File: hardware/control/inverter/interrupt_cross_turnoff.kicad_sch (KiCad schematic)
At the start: 17 parts, among them J1 RJ45, J2 RJ45, J3 RJ45, U1 L7812, U2 L7805, U3 74HC14, U4 74HC08, U5 74HC74

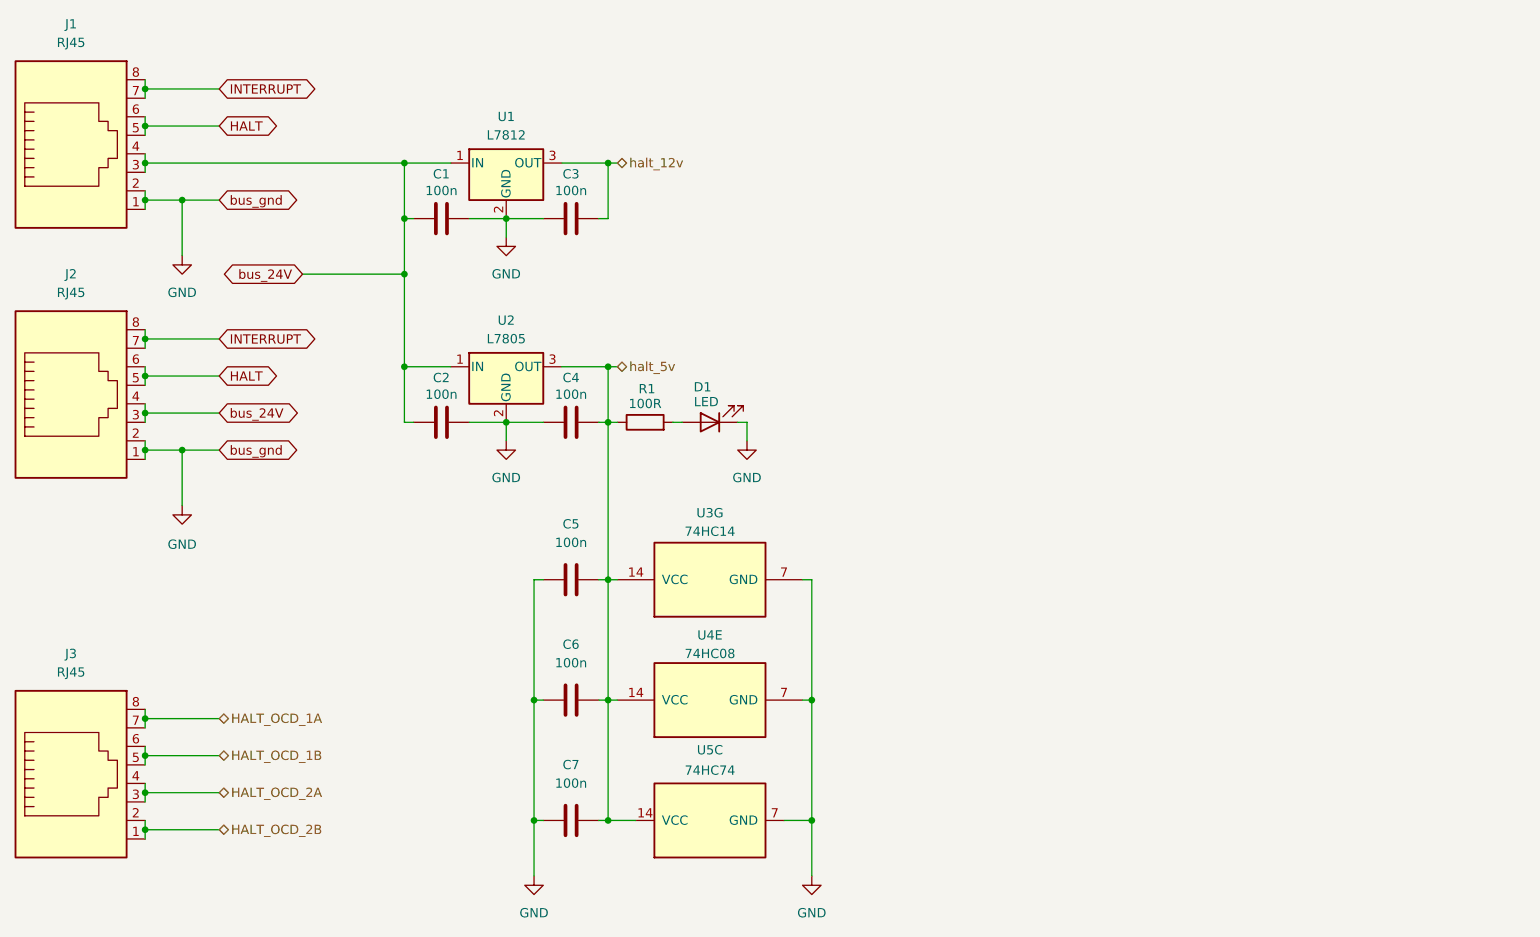
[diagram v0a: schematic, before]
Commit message: add progress on main drive controller and switch to hiearchical labels
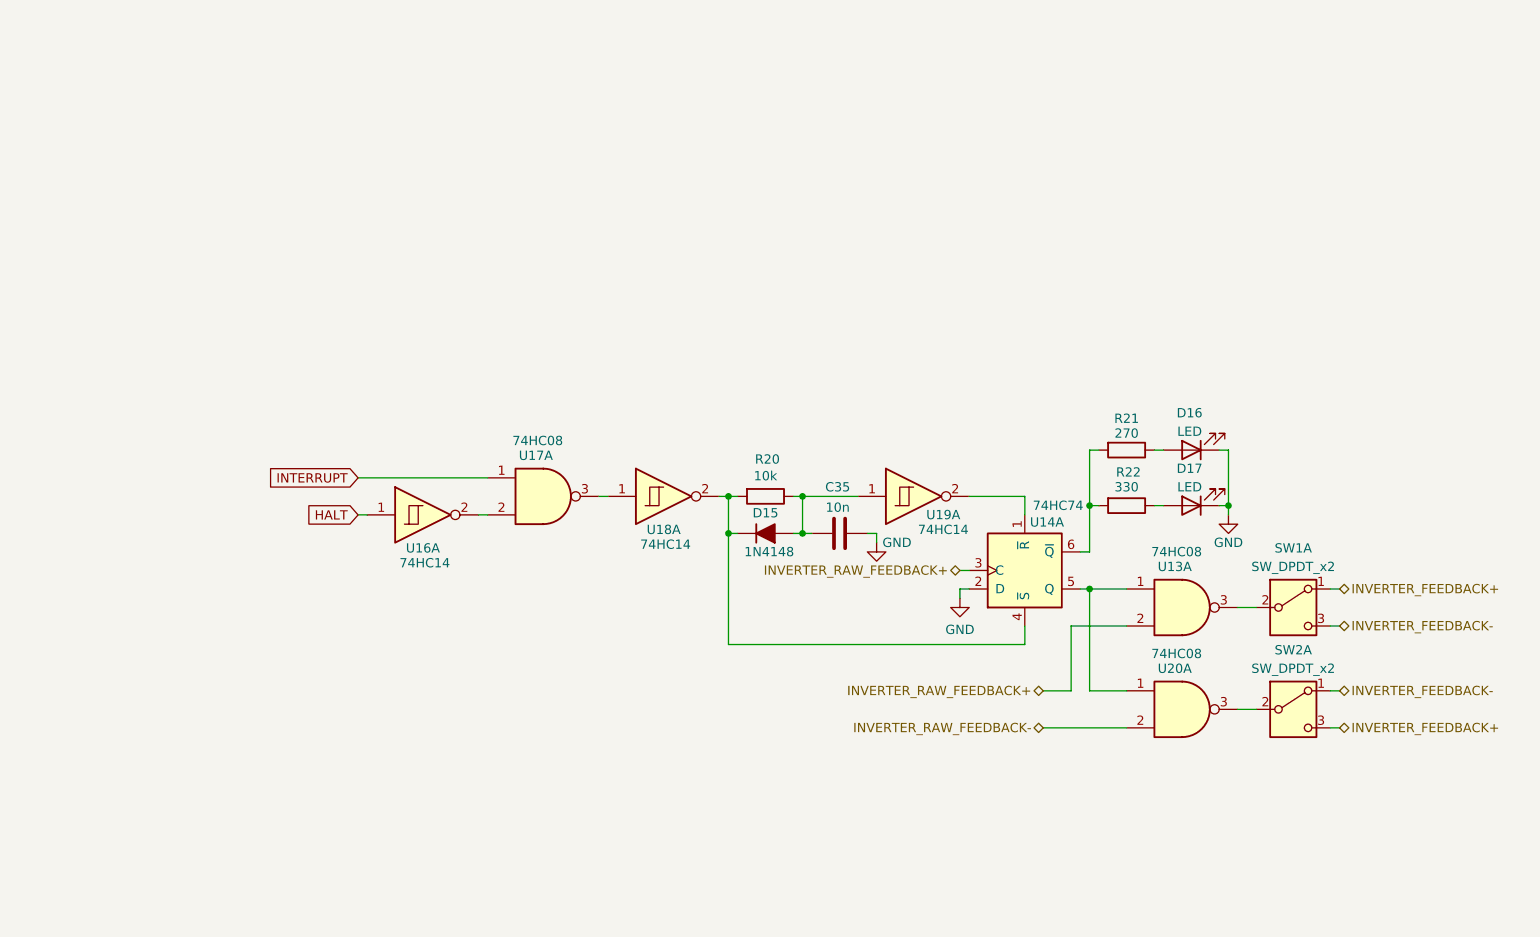
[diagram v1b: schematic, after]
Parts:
- removed C1, C2, C3, C4, C5, C6, C7: 100n, symbol Device:C
- removed D1: LED, symbol Device:LED
- removed J1, J2, J3: RJ45, symbol Connector:RJ45
- removed R1: 100R, symbol Device:R
- removed U1: L7812, symbol Regulator_Linear:L7812
- removed U2: L7805, symbol Regulator_Linear:L7805
- removed U3: 74HC14, symbol 74xx:74HC14
- removed U4: 74HC08, symbol 74xx:74HC00
- removed U5: 74HC74, symbol 74xx:74HC74
- added C35: 10n, symbol Device:C
- added D15: 1N4148, PCM_Diode_THT_AKL:D_DO-35_SOD27_P7.62mm_Horizontal, symbol PCM_Diode_AKL:1N4148
- added D16, D17: LED, symbol Device:LED
- added R20: 10k, symbol Device:R
- added R21: 270, symbol Device:R
- added R22: 330, symbol Device:R
- added SW1, SW2: SW_DPDT_x2, symbol Switch:SW_DPDT_x2
- added U13, U17, U20: 74HC08, symbol 74xx:74HC00
- added U14: 74HC74, symbol 74xx:74HC74
- added U16, U18, U19: 74HC14, symbol 74xx:74HC14
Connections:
- net GND: now also C35.2, D16.1 (K), D17.1 (K), U14.2 (D)
- net HALT: now also U16.1
- net INTERRUPT: now also U17.1
- new net: C35.1, D15.2 (A), R20.1, U19.1
- new net: D15.1 (K), R20.2, U14.4 (~{S}), U18.2
- new net: U13.1, U14.5 (Q), U20.1
- new net: SW2.2 (B), U20.3
- new net: D17.2 (A), R22.1
- new net: R21.2, R22.2, U14.6 (~{Q})
- new net: D16.2 (A), R21.1
- new net: U14.1 (~{R}), U19.2
- new net: SW1.2 (B), U13.3
- new net: U16.2, U17.2
- new net: U17.3, U18.1
- new net INVERTER_FEEDBACK+: SW1.1 (A), SW2.3 (C)
- new net INVERTER_FEEDBACK-: SW1.3 (C), SW2.1 (A)
- new net INVERTER_RAW_FEEDBACK+: U13.2, U14.3 (C)
- new net INVERTER_RAW_FEEDBACK-: U20.2
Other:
- company: Author: 9551 (devvie.cc) -> (none)
- title: QCW DRSSTC halt board input stage -> (none)

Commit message: update
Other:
- moved on the sheet: SW1A, SW2A, U13A, U20A
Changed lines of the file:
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@@
 	)
 	(junction
-		(at 167.64 102.87)
+		(at 167.64 111.76)
 		(diameter 0)
 		(color 0 0 0 0)
@@
 	(wire
 		(pts
-			(xy 167.64 102.87) (xy 167.64 116.84)
+			(xy 167.64 111.76) (xy 167.64 125.73)
 		)
 		(stroke
@@
 	(wire
 		(pts
+			(xy 167.64 102.87) (xy 166.37 102.87)
+		)
+		(stroke
+			(width 0)
+			(type default)
+		)
+	)
+	(wire
+		(pts
 			(xy 100.33 90.17) (xy 101.6 90.17)
 		)
@@
 	(wire
 		(pts
-			(xy 165.1 107.95) (xy 172.72 107.95)
-		)
-		(stroke
-			(width 0)
-			(type default)
-		)
-	)
-	(wire
-		(pts
 			(xy 118.11 90.17) (xy 119.38 90.17)
 		)
@@
 	(wire
 		(pts
-			(xy 166.37 102.87) (xy 167.64 102.87)
-		)
-		(stroke
-			(width 0)
-			(type default)
-		)
-	)
-	(wire
-		(pts
 			(xy 185.42 91.44) (xy 186.69 91.44)
 		)
@@
 	(wire
 		(pts
-			(xy 187.96 119.38) (xy 190.5 119.38)
+			(xy 184.15 128.27) (xy 186.69 128.27)
 		)
 		(stroke
@@
 	(wire
 		(pts
-			(xy 161.29 116.84) (xy 165.1 116.84)
+			(xy 161.29 116.84) (xy 168.91 116.84)
 		)
 		(stroke
@@
 	(wire
 		(pts
-			(xy 167.64 102.87) (xy 172.72 102.87)
+			(xy 167.64 111.76) (xy 168.91 111.76)
 		)
 		(stroke
@@
 	(wire
 		(pts
-			(xy 165.1 116.84) (xy 165.1 107.95)
-		)
-		(stroke
-			(width 0)
-			(type default)
-		)
-	)
-	(wire
-		(pts
 			(xy 138.43 95.25) (xy 138.43 96.52)
 		)
@@
 	(wire
 		(pts
-			(xy 167.64 116.84) (xy 172.72 116.84)
-		)
-		(stroke
-			(width 0)
-			(type default)
-		)
-	)
-	(wire
-		(pts
-			(xy 200.66 107.95) (xy 201.93 107.95)
-		)
-		(stroke
-			(width 0)
-			(type default)
-		)
-	)
-	(wire
-		(pts
-			(xy 200.66 121.92) (xy 201.93 121.92)
+			(xy 167.64 125.73) (xy 168.91 125.73)
+		)
+		(stroke
+			(width 0)
+			(type default)
+		)
+	)
+	(wire
+		(pts
+			(xy 196.85 116.84) (xy 198.12 116.84)
+		)
+		(stroke
+			(width 0)
+			(type default)
+		)
+	)
+	(wire
+		(pts
+			(xy 196.85 130.81) (xy 198.12 130.81)
 		)
 		(stroke
@@
 	(wire
 		(pts
-			(xy 200.66 102.87) (xy 201.93 102.87)
-		)
-		(stroke
-			(width 0)
-			(type default)
-		)
-	)
-	(wire
-		(pts
-			(xy 161.29 121.92) (xy 172.72 121.92)
+			(xy 167.64 111.76) (xy 167.64 102.87)
+		)
+		(stroke
+			(width 0)
+			(type default)
+		)
+	)
+	(wire
+		(pts
+			(xy 196.85 111.76) (xy 198.12 111.76)
+		)
+		(stroke
+			(width 0)
+			(type default)
+		)
+	)
+	(wire
+		(pts
+			(xy 161.29 130.81) (xy 168.91 130.81)
 		)
 		(stroke
@@
 	(wire
 		(pts
-			(xy 200.66 116.84) (xy 201.93 116.84)
-		)
-		(stroke
-			(width 0)
-			(type default)
-		)
-	)
-	(wire
-		(pts
-			(xy 187.96 105.41) (xy 190.5 105.41)
+			(xy 196.85 125.73) (xy 198.12 125.73)
+		)
+		(stroke
+			(width 0)
+			(type default)
+		)
+	)
+	(wire
+		(pts
+			(xy 184.15 114.3) (xy 186.69 114.3)
 		)
 		(stroke
@@
 	(hierarchical_label "INVERTER_RAW_FEEDBACK-"
 		(shape bidirectional)
-		(at 161.29 121.92 180)
+		(at 161.29 130.81 180)
 		(effects
 			(font
@@
 	(hierarchical_label "INVERTER_FEEDBACK+"
 		(shape bidirectional)
-		(at 201.93 102.87 0)
+		(at 198.12 111.76 0)
 		(effects
 			(font
@@
 	(hierarchical_label "INVERTER_FEEDBACK-"
 		(shape bidirectional)
-		(at 201.93 107.95 0)
+		(at 198.12 116.84 0)
 		(effects
 			(font
@@
 	(hierarchical_label "INVERTER_FEEDBACK+"
 		(shape bidirectional)
-		(at 201.93 121.92 0)
+		(at 198.12 130.81 0)
 		(effects
 			(font
@@
 	(hierarchical_label "INVERTER_FEEDBACK-"
 		(shape bidirectional)
-		(at 201.93 116.84 0)
+		(at 198.12 125.73 0)
 		(effects
 			(font
@@
 	(symbol
 		(lib_id "74xx:74HC00")
-		(at 180.34 119.38 0)
+		(at 176.53 128.27 0)
 		(unit 1)
 		(exclude_from_sim no)
@@
 		(dnp no)
 		(property "Reference" "U20"
-			(at 179.324 113.792 0)
+			(at 175.514 122.682 0)
 			(effects
 				(font
@@
 		)
 		(property "Value" "74HC08"
-			(at 179.578 111.76 0)
+			(at 175.768 120.65 0)
 			(effects
 				(font
@@
 		)
 		(property "Footprint" ""
-			(at 180.34 119.38 0)
+			(at 176.53 128.27 0)
 			(effects
 				(font
@@
 		)
 		(property "Datasheet" "http://www.ti.com/lit/gpn/sn74hc00"
-			(at 180.34 119.38 0)
+			(at 176.53 128.27 0)
 			(effects
 				(font
@@
 		)
 		(property "Description" "quad 2-input NAND gate"
-			(at 180.34 119.38 0)
+			(at 176.53 128.27 0)
 			(effects
 				(font
@@
 	(symbol
 		(lib_id "Switch:SW_DPDT_x2")
-		(at 195.58 119.38 0)
+		(at 191.77 128.27 0)
 		(unit 1)
 		(exclude_from_sim no)
@@
 		(dnp no)
 		(property "Reference" "SW2"
-			(at 195.58 111.252 0)
+			(at 191.77 120.142 0)
 			(effects
 				(font
@@
 		)
 		(property "Value" "SW_DPDT_x2"
-			(at 195.58 113.792 0)
+			(at 191.77 122.682 0)
 			(effects
 				(font
@@
 		)
 		(property "Footprint" ""
-			(at 195.58 119.38 0)
+			(at 191.77 128.27 0)
 			(effects
 				(font
@@
 		)
 		(property "Datasheet" "~"
-			(at 195.58 119.38 0)
+			(at 191.77 128.27 0)
 			(effects
 				(font
@@
 		)
 		(property "Description" "Switch, dual pole double throw, separate symbols"
-			(at 195.58 119.38 0)
+			(at 191.77 128.27 0)
 			(effects
 				(font
@@
 	(symbol
 		(lib_id "74xx:74HC00")
-		(at 180.34 105.41 0)
+		(at 176.53 114.3 0)
 		(unit 1)
 		(exclude_from_sim no)
@@
 		(dnp no)
 		(property "Reference" "U13"
-			(at 179.324 99.822 0)
+			(at 175.514 108.712 0)
 			(effects
 				(font
@@
 		)
 		(property "Value" "74HC08"
-			(at 179.578 97.79 0)
+			(at 175.768 106.68 0)
 			(effects
 				(font
@@
 		)
 		(property "Footprint" ""
-			(at 180.34 105.41 0)
+			(at 176.53 114.3 0)
 			(effects
 				(font
@@
 		)
 		(property "Datasheet" "http://www.ti.com/lit/gpn/sn74hc00"
-			(at 180.34 105.41 0)
+			(at 176.53 114.3 0)
 			(effects
 				(font
@@
 		)
 		(property "Description" "quad 2-input NAND gate"
-			(at 180.34 105.41 0)
+			(at 176.53 114.3 0)
 			(effects
 				(font
@@
 	(symbol
 		(lib_id "Switch:SW_DPDT_x2")
-		(at 195.58 105.41 0)
+		(at 191.77 114.3 0)
 		(unit 1)
 		(exclude_from_sim no)
@@
 		(dnp no)
 		(property "Reference" "SW1"
-			(at 195.58 97.282 0)
+			(at 191.77 106.172 0)
 			(effects
 				(font
@@
 		)
 		(property "Value" "SW_DPDT_x2"
-			(at 195.58 99.822 0)
+			(at 191.77 108.712 0)
 			(effects
 				(font
@@
 		)
 		(property "Footprint" ""
-			(at 195.58 105.41 0)
+			(at 191.77 114.3 0)
 			(effects
 				(font
@@
 		)
 		(property "Datasheet" "~"
-			(at 195.58 105.41 0)
+			(at 191.77 114.3 0)
 			(effects
 				(font
@@
 		)
 		(property "Description" "Switch, dual pole double throw, separate symbols"
-			(at 195.58 105.41 0)
-			(effects
-				(font
+			(at 191.77 114.3 0)
+			(effects
+				(font

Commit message: update right about freaking everything
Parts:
- removed SW1, SW2: SW_DPDT_x2, symbol Switch:SW_DPDT_x2
- removed U13, U17, U20: 74HC08, symbol 74xx:74HC00
- added U13: 74LS08, symbol 74xx:74LS08
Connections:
- net INTERRUPT: now also U13.1
- net INVERTER_RUN_STATE: now reaches U14.5 (Q)
- net INVERTER_RUN_STATE: now also R21.2
- net at R22.2, U14.6 (~{Q}): no longer R21.2
- net at U16.2: now also U13.2
- net at U18.1: now also U13.3
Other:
- moved on the sheet: D16, D17, R21, R22

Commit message: idk some changes
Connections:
- net INVERTER_RUN_STATE: no longer names the net of R21.2, U14.5 (Q)
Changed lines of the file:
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@@
 		(color 0 0 0 0)
 	)
-	(junction
-		(at 180.34 102.87)
-		(diameter 0)
-		(color 0 0 0 0)
-	)
 	(wire
 		(pts
@@
 		(pts
 			(xy 151.13 90.17) (xy 158.75 90.17)
-		)
-		(stroke
-			(width 0)
-			(type default)
-		)
-	)
-	(wire
-		(pts
-			(xy 181.61 102.87) (xy 180.34 102.87)
 		)
 		(stroke
@@
 		)
 	)
-	(hierarchical_label "INVERTER_RUN_STATE"
-		(shape bidirectional)
-		(at 181.61 102.87 0)
-		(effects
-			(font
-				(size 1.27 1.27)
-			)
-			(justify left)
-		)
-	)

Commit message: completed-ish inverter board, probably not, but anyway
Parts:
- added U10, U11: 74LS08, symbol 74xx:74LS08
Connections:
- net INVERTER_RAW_FEEDBACK+: now also U10.2
- net at R21.2, U14.5 (Q): now also U10.1, U11.1
- new net INVERTER_FEEDBACK+: U10.3
- new net INVERTER_FEEDBACK-: U11.3
- new net INVERTER_RAW_FEEDBACK-: U11.2
